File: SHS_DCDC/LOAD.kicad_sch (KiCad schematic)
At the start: 30 parts, among them Q2 PMV100XPEAR, Q3 2N7002, Q4 2N7002, Q5 PMV100XPEAR, Q6 2N7002, Q7 PMV100XPEAR

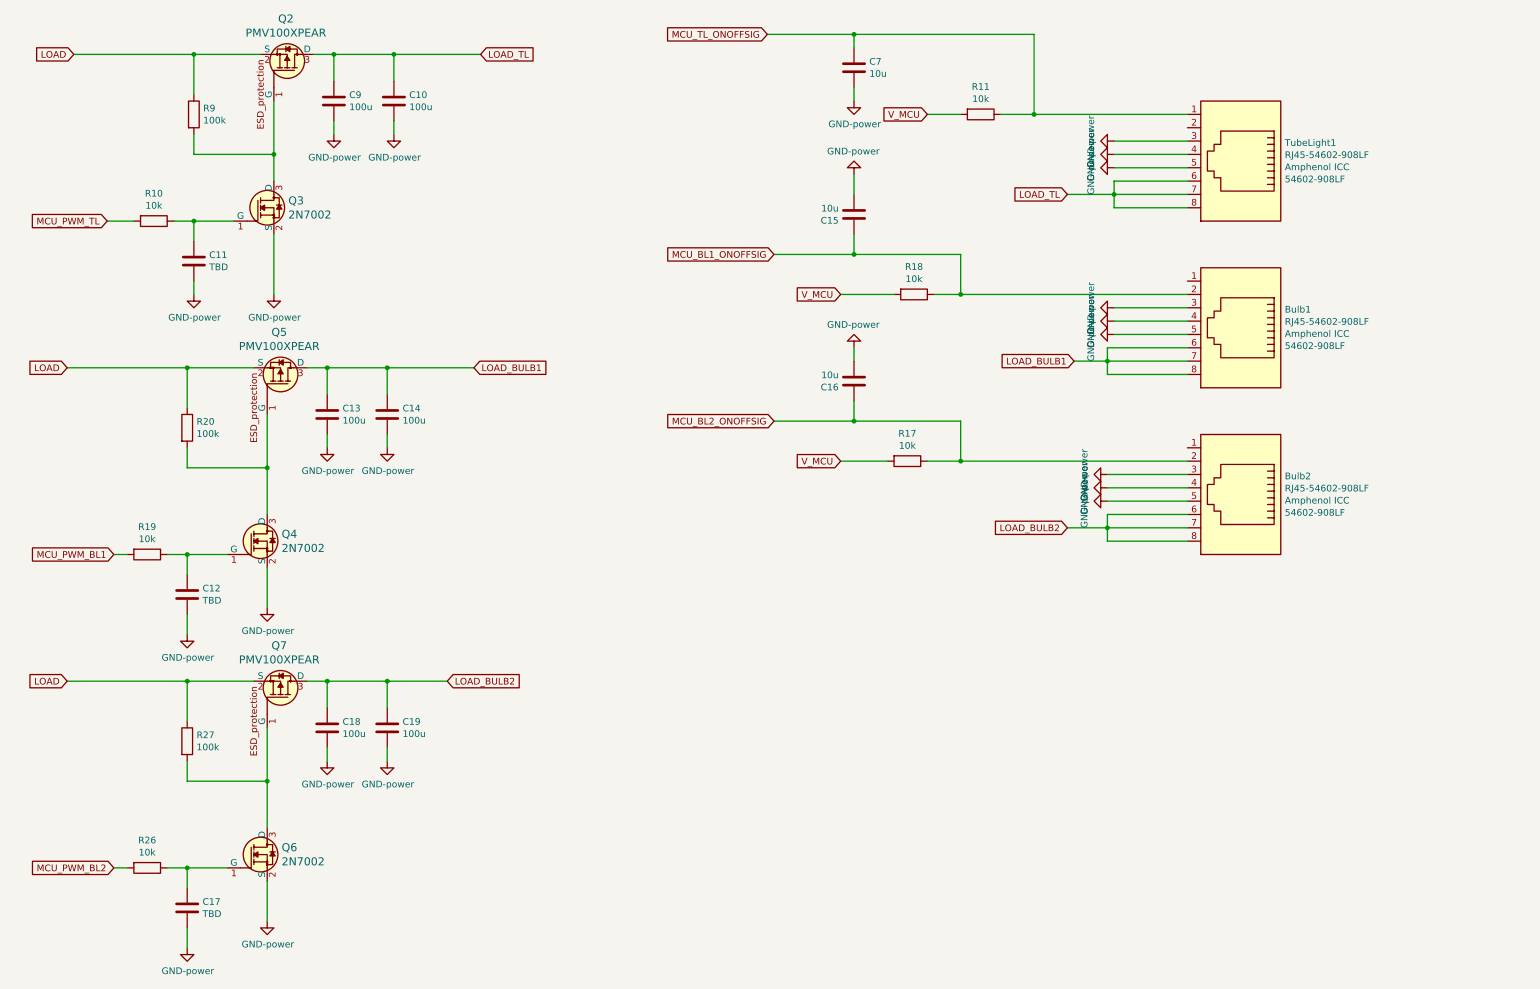
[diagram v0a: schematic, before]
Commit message: OCP
Adding overcharge protection
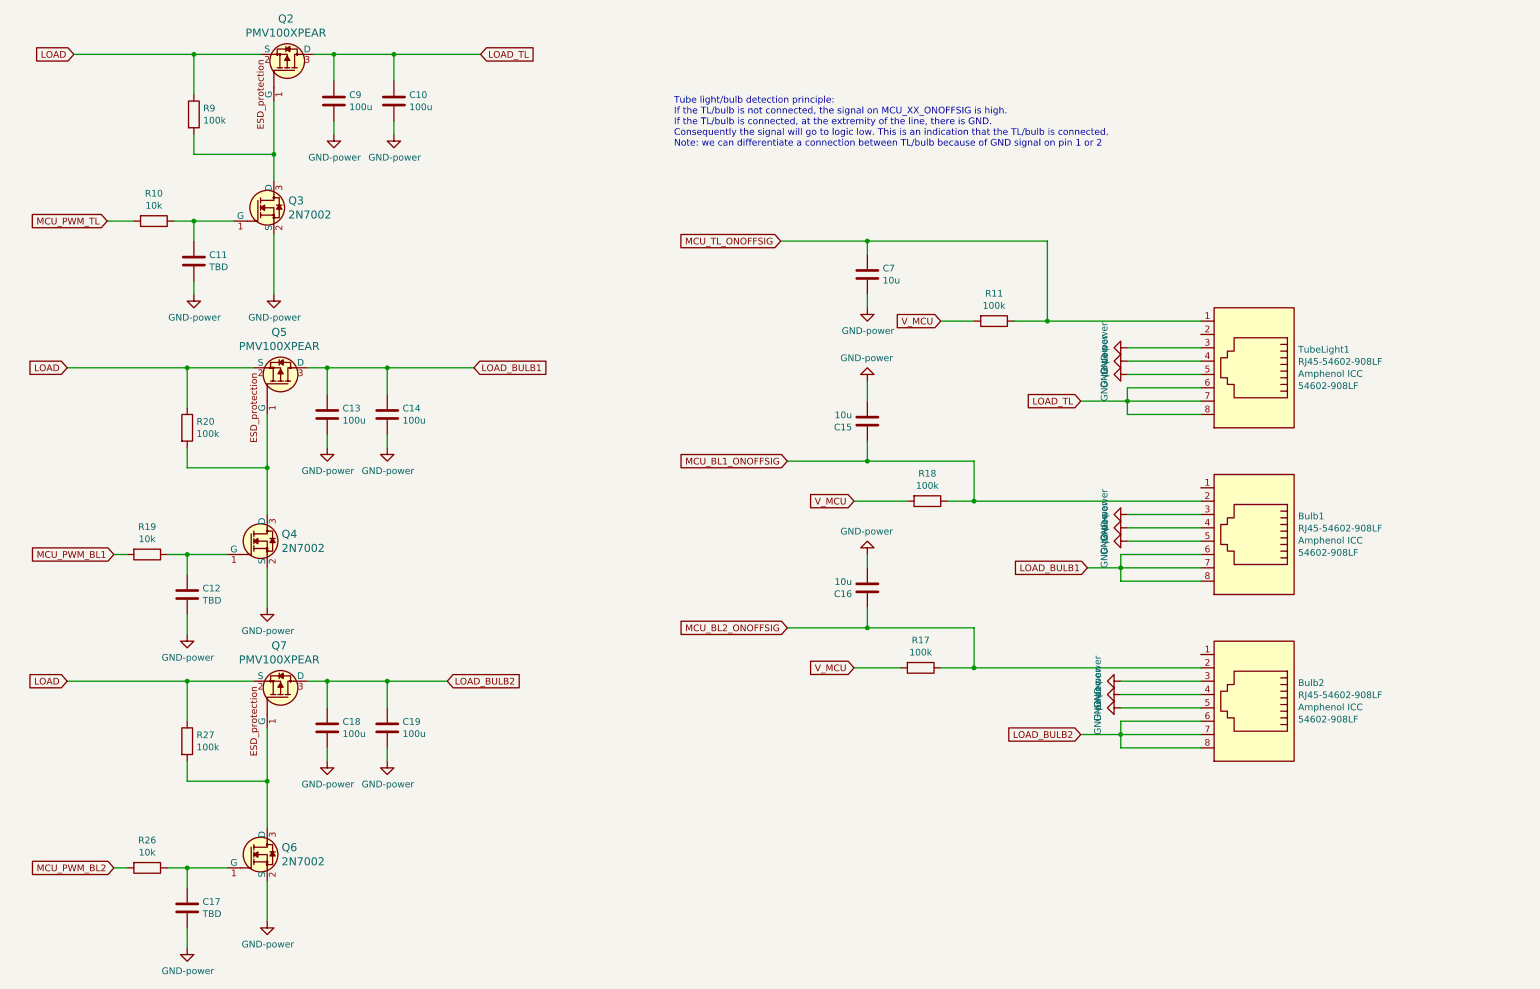
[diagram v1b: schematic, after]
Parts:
- R11, R17, R18: value 10k -> 100k
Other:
- note added: "Tube light/bulb detection principle: If the TL/bulb is not connected, the signal on MCU_XX_ONOFFSIG is high. If the TL/bulb is connected, at the extremity of the line, there is GND. Consequently the signal will go to logic low. This is an indication that the TL/bulb is connected. Note: we can differentiate a connection between TL/bulb because of GND signal on pin 1 or 2"
- moved on the sheet: Bulb1, Bulb2, C15, C16, C7, R11, R17, R18, TubeLight1

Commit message: DFU update
PCB update to setup 3 ways of FW/Debug capability:
1. JTAG (FW & Debug)
2. USB DFU (FW & Debug)
3. UART (FW only)
With BOOT0 button installed too
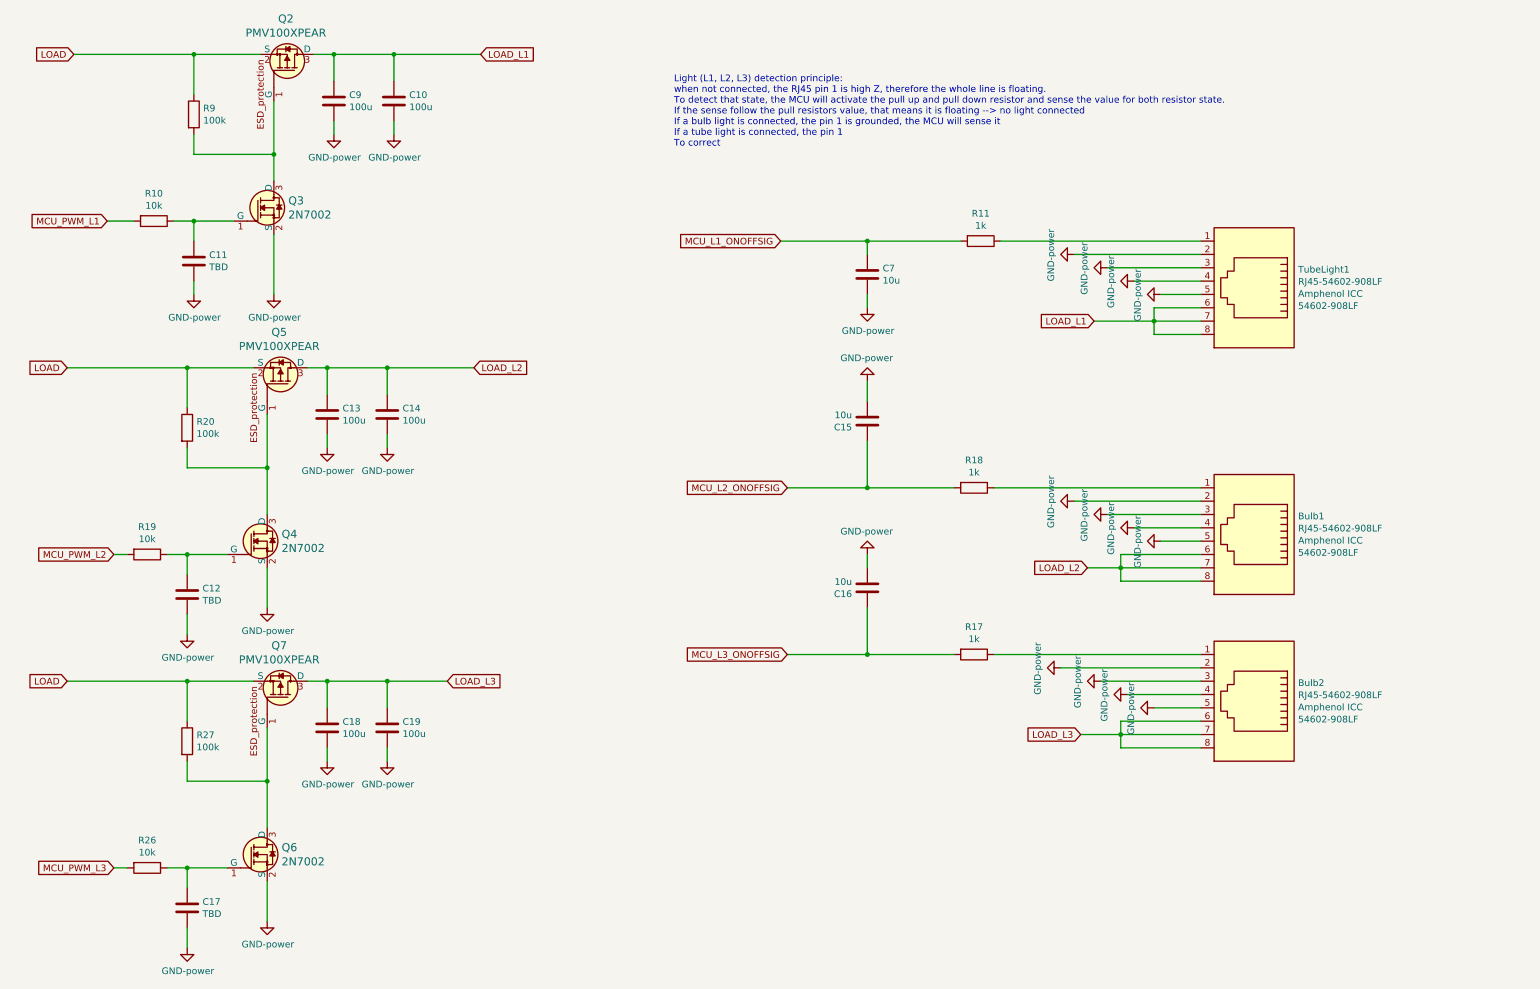
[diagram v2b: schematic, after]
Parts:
- R11, R17, R18: value 100k -> 1k
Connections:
- net GND: now also Bulb1.2, Bulb2.2, TubeLight1.2
- net at Bulb1.1: now also R18.1
- net at Bulb2.1: now also R17.1
- net LOAD_BULB1 renamed LOAD_L2
- net LOAD_BULB2 renamed LOAD_L3
- net LOAD_TL renamed LOAD_L1
- removed net MCU_BL1_ONOFFSIG: Bulb1.2, C15.1, R18.1
- removed net MCU_BL2_ONOFFSIG: Bulb2.2, C16.1, R17.1
- net MCU_PWM_BL1 renamed MCU_PWM_L2
- net MCU_PWM_BL2 renamed MCU_PWM_L3
- net MCU_PWM_TL renamed MCU_PWM_L1
- net MCU_TL_ONOFFSIG: no longer names the net of R11.1, TubeLight1.1
- net MCU_TL_ONOFFSIG: no longer C7.1
- removed net V_MCU: R11.2, R17.2, R18.2
- new net MCU_L1_ONOFFSIG: C7.1, R11.2
- new net MCU_L2_ONOFFSIG: C15.1, R18.2
- new net MCU_L3_ONOFFSIG: C16.1, R17.2
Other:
- note added: "Light (L1, L2, L3) detection principle: when not connected, the RJ45 pin 1 is high Z, therefore the whole line is floating. To detect that state, the MCU will activate the pull up and pull down resistor and sense the value for both resistor state. If the sense follow the pull resistors value, that means it is floating --> no light connected If a bulb light is connected, the pin 1 is grounded, the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"
- note removed: "Tube light/bulb detection principle: If the TL/bulb is not connected, the signal on MCU_XX_ONOFFSIG is high. If the TL/bulb is connected, at the extremity of the line, there is GND. Consequently the signal will go to logic low. This is an indication that the TL/bulb is connected. Note: we can differentiate a connection between TL/bulb because of GND signal on pin 1 or 2"
- moved on the sheet: R17, R18, TubeLight1

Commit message: PV input Power
Big modification on the PV input power protection, precisely on the reverse battery current protection, and also on the switch between direct PV charging and the DCDC converter
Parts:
- added C44, C45, C46: 1uF, Capacitor_SMD:C_0402_1005Metric, symbol Device:C
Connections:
- net GND: now also C44.2, C45.2, C46.2
- net LOAD_L1: now also C46.1
- net LOAD_L2: now also C44.1
- net LOAD_L3: now also C45.1
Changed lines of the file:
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@@
   (junction (at 59.69 160.02) (diameter 0) (color 0 0 0 0)
   )
+  (junction (at 93.98 140.97) (diameter 0) (color 0 0 0 0)
+  )
   (junction (at 45.72 53.34) (diameter 0) (color 0 0 0 0)
   )
@@
   (junction (at 173.99 57.15) (diameter 0) (color 0 0 0 0)
   )
+  (junction (at 93.98 81.28) (diameter 0) (color 0 0 0 0)
+  )
   (junction (at 59.69 100.33) (diameter 0) (color 0 0 0 0)
   )
@@
   (junction (at 82.55 81.28) (diameter 0) (color 0 0 0 0)
   )
+  (junction (at 95.25 21.59) (diameter 0) (color 0 0 0 0)
+  )
   (junction (at 44.45 116.84) (diameter 0) (color 0 0 0 0)
   )
@@
     (stroke (width 0) (type default) (color 0 0 0 0))
   )
+  (wire (pts (xy 93.98 93.98) (xy 93.98 96.52))
+    (stroke (width 0) (type default) (color 0 0 0 0))
+  )
   (wire (pts (xy 44.45 187.96) (xy 44.45 191.77))
     (stroke (width 0) (type default) (color 0 0 0 0))
@@
     (stroke (width 0) (type default) (color 0 0 0 0))
   )
+  (wire (pts (xy 95.25 34.29) (xy 95.25 36.83))
+    (stroke (width 0) (type default) (color 0 0 0 0))
+  )
+  (wire (pts (xy 93.98 81.28) (xy 99.06 81.28))
+    (stroke (width 0) (type default) (color 0 0 0 0))
+  )
   (wire (pts (xy 237.49 109.22) (xy 219.71 109.22))
     (stroke (width 0) (type default) (color 0 0 0 0))
@@
     (stroke (width 0) (type default) (color 0 0 0 0))
   )
+  (wire (pts (xy 93.98 153.67) (xy 93.98 156.21))
+    (stroke (width 0) (type default) (color 0 0 0 0))
+  )
   (wire (pts (xy 237.49 67.31) (xy 229.87 67.31))
     (stroke (width 0) (type default) (color 0 0 0 0))
@@
     (stroke (width 0) (type default) (color 0 0 0 0))
   )
+  (wire (pts (xy 93.98 140.97) (xy 93.98 146.05))
+    (stroke (width 0) (type default) (color 0 0 0 0))
+  )
   (wire (pts (xy 173.99 135.89) (xy 158.75 135.89))
     (stroke (width 0) (type default) (color 0 0 0 0))
@@
     (stroke (width 0) (type default) (color 0 0 0 0))
   )
+  (wire (pts (xy 95.25 21.59) (xy 95.25 26.67))
+    (stroke (width 0) (type default) (color 0 0 0 0))
+  )
   (wire (pts (xy 213.36 59.69) (xy 237.49 59.69))
     (stroke (width 0) (type default) (color 0 0 0 0))
@@
     (stroke (width 0) (type default) (color 0 0 0 0))
   )
-  (wire (pts (xy 83.82 21.59) (xy 100.33 21.59))
+  (wire (pts (xy 95.25 21.59) (xy 100.33 21.59))
+    (stroke (width 0) (type default) (color 0 0 0 0))
+  )
+  (wire (pts (xy 83.82 21.59) (xy 95.25 21.59))
     (stroke (width 0) (type default) (color 0 0 0 0))
   )
@@
     (stroke (width 0) (type default) (color 0 0 0 0))
   )
+  (wire (pts (xy 93.98 81.28) (xy 93.98 86.36))
+    (stroke (width 0) (type default) (color 0 0 0 0))
+  )
   (wire (pts (xy 67.31 140.97) (xy 71.12 140.97))
     (stroke (width 0) (type default) (color 0 0 0 0))
@@
     (stroke (width 0) (type default) (color 0 0 0 0))
   )
-  (wire (pts (xy 82.55 81.28) (xy 99.06 81.28))
+  (wire (pts (xy 82.55 81.28) (xy 93.98 81.28))
     (stroke (width 0) (type default) (color 0 0 0 0))
   )
@@
   )
   (wire (pts (xy 215.9 119.38) (xy 222.25 119.38))
+    (stroke (width 0) (type default) (color 0 0 0 0))
+  )
+  (wire (pts (xy 93.98 140.97) (xy 101.6 140.97))
     (stroke (width 0) (type default) (color 0 0 0 0))
   )
@@
     )
   )
-  (global_label "LOAD_L3" (shape input) (at 93.98 140.97 0) (fields_autoplaced)
+  (global_label "LOAD_L3" (shape input) (at 101.6 140.97 0) (fields_autoplaced)
     (effects (font (size 1.27 1.27)) (justify left))
-    (property "Intersheet References" "${INTERSHEET_REFS}" (id 0) (at 104.2266 140.8906 0)
+    (property "Intersheet References" "${INTERSHEET_REFS}" (id 0) (at 111.8466 140.8906 0)
       (effects (font (size 1.27 1.27)) (justify left) hide)
     )
@@
     (pin "1")
   )
+  (symbol (lib_id "SHS_DCDC:GND-power") (at 93.98 96.52 0) (unit 1)
+    (in_bom yes) (on_board yes)
+    (property "Reference" "#PWR074" (id 0) (at 93.98 102.87 0)
+      (effects (font (size 1.27 1.27)) hide)
+    )
+    (property "Value" "GND-power" (id 1) (at 94.107 100.9142 0))
+    (property "Footprint" "" (id 2) (at 93.98 96.52 0)
+      (effects (font (size 1.27 1.27)) hide)
+    )
+    (property "Datasheet" "" (id 3) (at 93.98 96.52 0)
+      (effects (font (size 1.27 1.27)) hide)
+    )
+    (pin "1")
+  )
   (symbol (lib_id "SHS_DCDC:GND-power") (at 213.36 106.68 270) (unit 1)
     (in_bom yes) (on_board yes)
@@
     )
     (pin "1")
+  )
+  (symbol (lib_id "Device:C") (at 93.98 149.86 0) (unit 1)
+    (in_bom yes) (on_board yes) (fields_autoplaced)
+    (property "Reference" "C45" (id 0) (at 97.79 148.5899 0)
+      (effects (font (size 1.27 1.27)) (justify left))
+    )
+    (property "Value" "1uF" (id 1) (at 97.79 151.1299 0)
+      (effects (font (size 1.27 1.27)) (justify left))
+    )
+    (property "Footprint" "Capacitor_SMD:C_0402_1005Metric" (id 2) (at 94.9452 153.67 0)
+      (effects (font (size 1.27 1.27)) hide)
+    )
+    (property "Datasheet" "~" (id 3) (at 93.98 149.86 0)
+      (effects (font (size 1.27 1.27)) hide)
+    )
+    (pin "1")
+    (pin "2")
   )
   (symbol (lib_id "SHS_DCDC:R-Device") (at 195.58 57.15 270) (unit 1)
@@
     (pin "2")
   )
+  (symbol (lib_id "SHS_DCDC:GND-power") (at 93.98 156.21 0) (unit 1)
+    (in_bom yes) (on_board yes)
+    (property "Reference" "#PWR075" (id 0) (at 93.98 162.56 0)
+      (effects (font (size 1.27 1.27)) hide)
+    )
+    (property "Value" "GND-power" (id 1) (at 94.107 160.6042 0))
+    (property "Footprint" "" (id 2) (at 93.98 156.21 0)
+      (effects (font (size 1.27 1.27)) hide)
+    )
+    (property "Datasheet" "" (id 3) (at 93.98 156.21 0)
+      (effects (font (size 1.27 1.27)) hide)
+    )
+    (pin "1")
+  )
+  (symbol (lib_id "SHS_DCDC:GND-power") (at 95.25 36.83 0) (unit 1)
+    (in_bom yes) (on_board yes)
+    (property "Reference" "#PWR076" (id 0) (at 95.25 43.18 0)
+      (effects (font (size 1.27 1.27)) hide)
+    )
+    (property "Value" "GND-power" (id 1) (at 95.377 41.2242 0))
+    (property "Footprint" "" (id 2) (at 95.25 36.83 0)
+      (effects (font (size 1.27 1.27)) hide)
+    )
+    (property "Datasheet" "" (id 3) (at 95.25 36.83 0)
+      (effects (font (size 1.27 1.27)) hide)
+    )
+    (pin "1")
+  )
+  (symbol (lib_id "Device:C") (at 93.98 90.17 0) (unit 1)
+    (in_bom yes) (on_board yes) (fields_autoplaced)
+    (property "Reference" "C44" (id 0) (at 97.79 88.8999 0)
+      (effects (font (size 1.27 1.27)) (justify left))
+    )
+    (property "Value" "1uF" (id 1) (at 97.79 91.4399 0)
+      (effects (font (size 1.27 1.27)) (justify left))
+    )
+    (property "Footprint" "Capacitor_SMD:C_0402_1005Metric" (id 2) (at 94.9452 93.98 0)
+      (effects (font (size 1.27 1.27)) hide)
+    )
+    (property "Datasheet" "~" (id 3) (at 93.98 90.17 0)
+      (effects (font (size 1.27 1.27)) hide)
+    )
+    (pin "1")
+    (pin "2")
+  )
   (symbol (lib_id "SHS_DCDC:GND-power") (at 210.82 138.43 270) (unit 1)
     (in_bom yes) (on_board yes)
@@
     (pin "1")
   )
+  (symbol (lib_id "Device:C") (at 95.25 30.48 0) (unit 1)
+    (in_bom yes) (on_board yes) (fields_autoplaced)
+    (property "Reference" "C46" (id 0) (at 99.06 29.2099 0)
+      (effects (font (size 1.27 1.27)) (justify left))
+    )
+    (property "Value" "1uF" (id 1) (at 99.06 31.7499 0)
+      (effects (font (size 1.27 1.27)) (justify left))
+    )
+    (property "Footprint" "Capacitor_SMD:C_0402_1005Metric" (id 2) (at 96.2152 34.29 0)
+      (effects (font (size 1.27 1.27)) hide)
+    )
+    (property "Datasheet" "~" (id 3) (at 95.25 30.48 0)
+      (effects (font (size 1.27 1.27)) hide)
+    )
+    (pin "1")
+    (pin "2")
+  )
 )
